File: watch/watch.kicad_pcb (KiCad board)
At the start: 2 copper layers, 92 parts, among them Q1 Q_NMOS_GSD, Q2 Q_NMOS_GSD, Q3 Q_NMOS_GSD, Q4 Q_NMOS_GSD, U1 STM32L071CBTx, Y1 Crystal

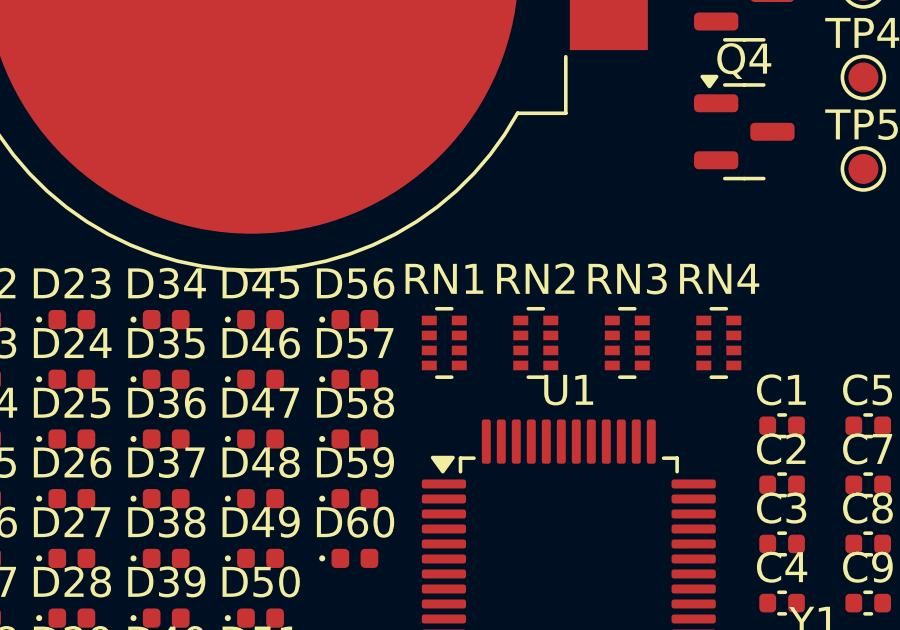
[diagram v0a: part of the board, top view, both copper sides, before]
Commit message: added unfinished footprint for DFN0606 FETs
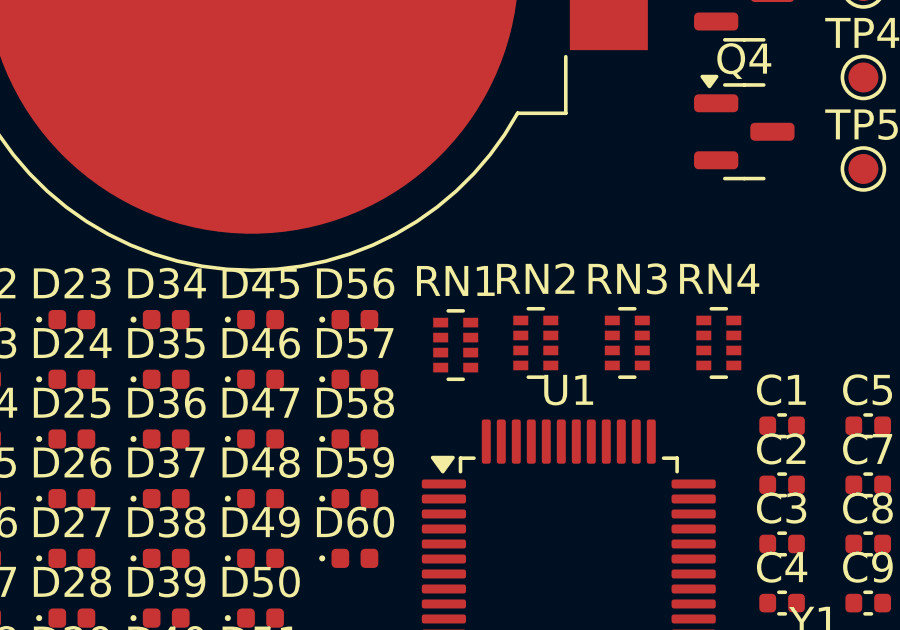
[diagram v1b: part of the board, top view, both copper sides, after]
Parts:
- moved RN1 0.39 mm to (159.8, 100.9)
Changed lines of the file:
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@@
 	(footprint "Resistor_SMD:R_Array_Concave_4x0402"
 		(layer "F.Cu")
-		(at 159.37 100.83)
+		(at 159.75 100.9)
 		(descr "Thick Film Chip Resistor Array, Wave soldering, Vishay CRA04P (see cra04p.pdf)")
 		(tags "resistor array")

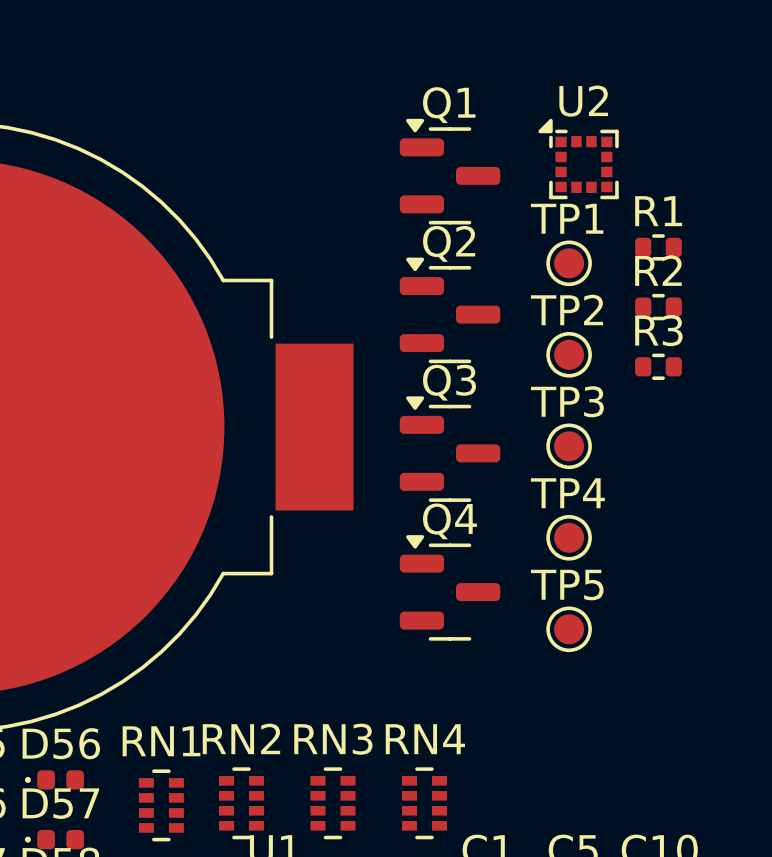
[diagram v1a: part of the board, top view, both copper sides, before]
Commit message: added DFN0606 footprint
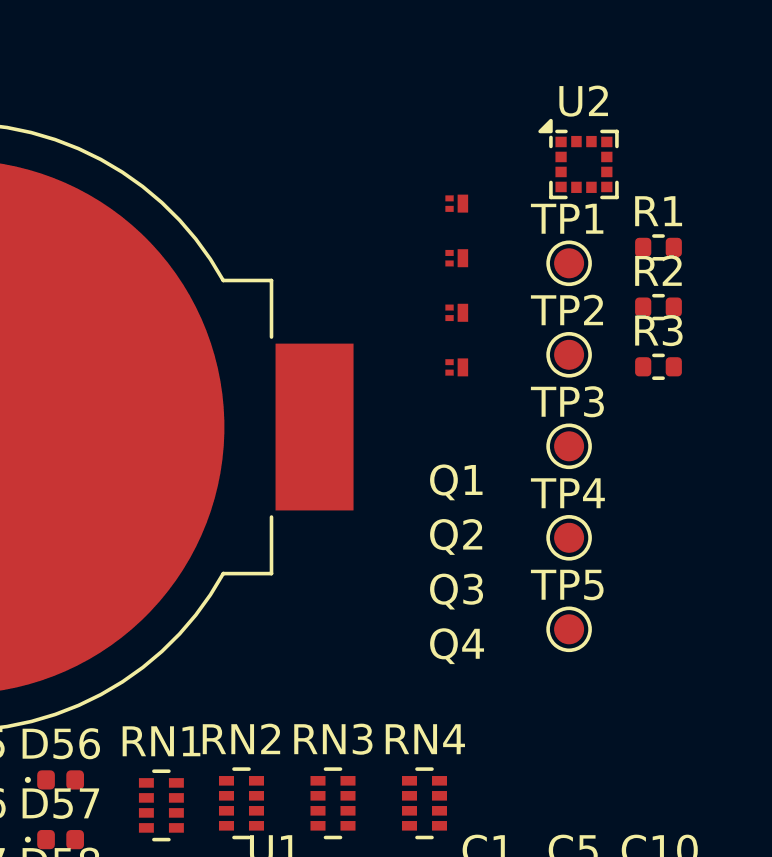
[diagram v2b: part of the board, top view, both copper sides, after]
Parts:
- Q1, Q2, Q3, Q4: value Q_NMOS_GSD -> DMN2991UFZ; footprint Package_TO_SOT_SMD:SOT-23 -> DFN0603:DFN0606
- moved Q4 7.49 mm to (169.6, 86.3)
- moved Q3 4.69 mm to (169.6, 84.5)
- moved Q2 1.89 mm to (169.6, 82.7)
- moved Q1 0.95 mm to (169.6, 80.8)

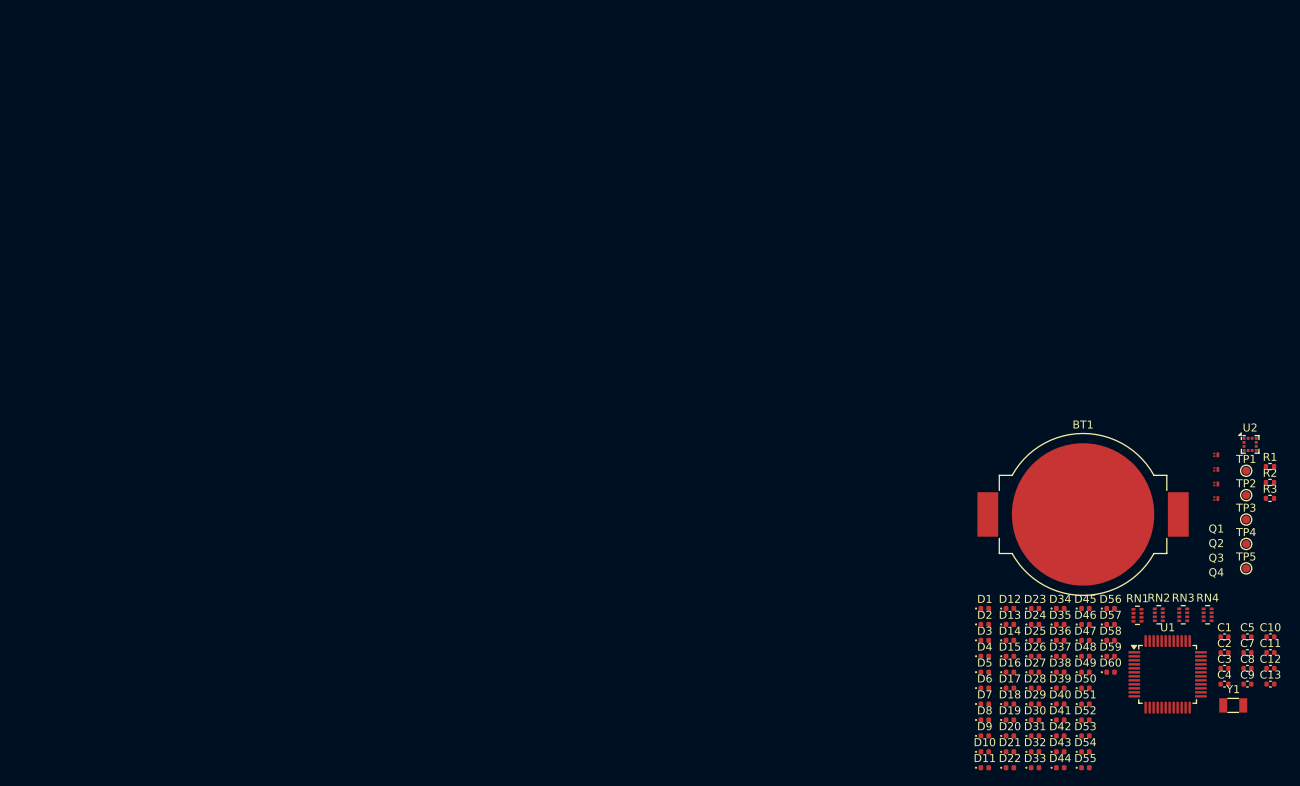
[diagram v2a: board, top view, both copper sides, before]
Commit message: removed low side FETs, started PCB
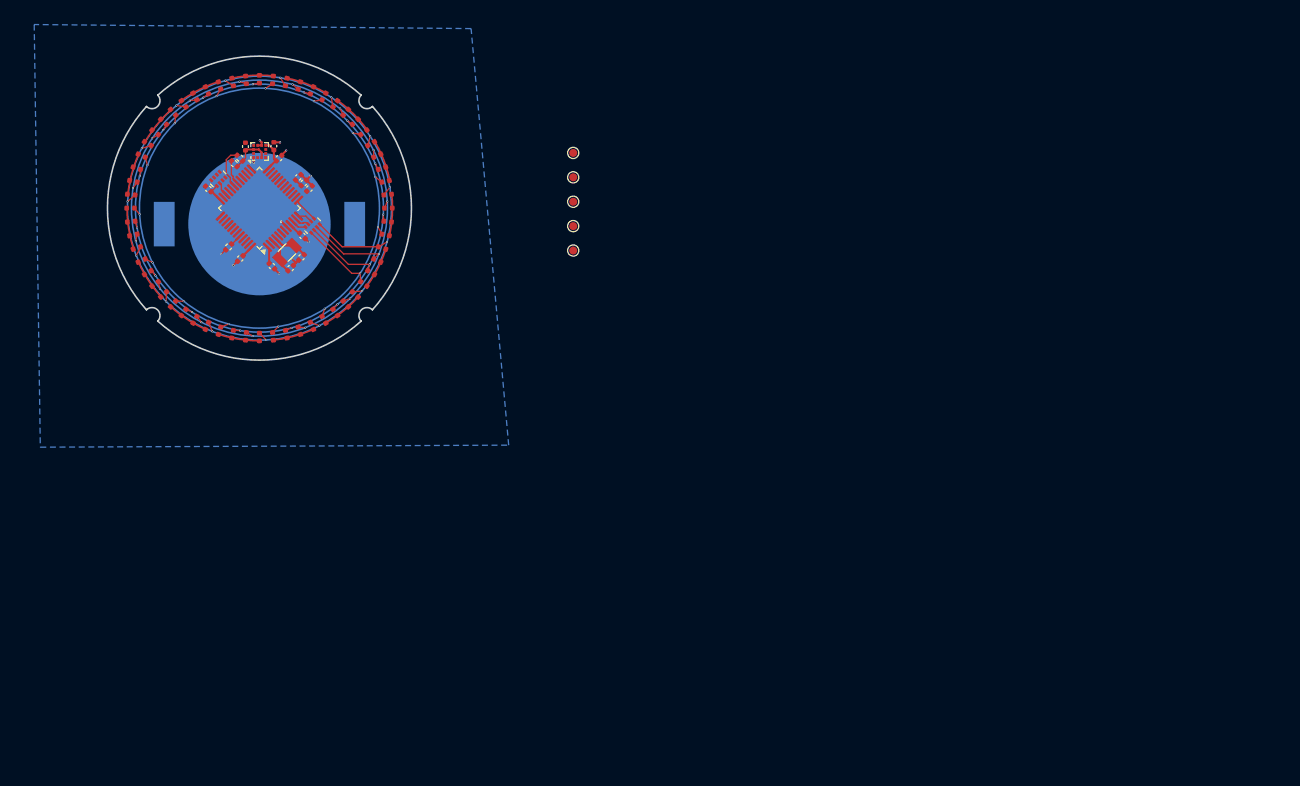
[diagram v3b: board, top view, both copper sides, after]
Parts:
- removed Q1, Q2, Q3, Q4: DMN2991UFZ, DFN0603:DFN0606
- removed RN2: 1M, Resistor_SMD:R_Array_Concave_4x0402
- removed RN3: 22, Resistor_SMD:R_Array_Concave_4x0402
- BT1: moved to B.Cu
- D1, D10, D11, D12, D13, D14, D15, D16, D17, D18, D19, D2, D20, D21, D22, D23, D24, D25, D26, D27, D28, D29, D3, D30, D31, D32, D33, D34, D35, D36, D37, D38, D39, D4, D40, D41, D42, D43, D44, D45, D46, D47, D48, D49, D5, D50, D51, D52, D53, D54, D55, D56, D57, D58, D59, D6, D60, D7, D8, D9: footprint LED_SMD:LED_0402_1005Metric -> LED_Without_Dot:LED402_without_dot
- RN1: value 1k -> 100
- Y1: value Crystal -> 3131M-32.768DTTLRRL
- moved C9 142.1 mm to (48.2, 42.3), turned to -90 degrees
- moved C4 141.3 mm to (43.6, 47.6), turned to -45 degrees
- moved C10 138.9 mm to (51.8, 42.2), turned to -90 degrees
- moved C12 136.1 mm to (54.9, 46.1), turned to -135 degrees
- moved C13 136.1 mm to (55.5, 46.9), turned to -135 degrees
- moved RN4 135.1 mm to (44.9, 46.4), turned to 135 degrees
- moved R2 135.0 mm to (47.5, 43.8), turned to 135 degrees
- moved R1 134.9 mm to (46.9, 44.5), turned to 135 degrees
- moved C5 134.5 mm to (47.6, 56.3), turned to 45 degrees
- moved C3 134.3 mm to (52.5, 43.8), turned to -135 degrees
- moved R3 133.9 mm to (46.1, 54.9), turned to -135 degrees
- moved C11 133.4 mm to (56.2, 47.5), turned to -135 degrees
- moved Y1 131.1 mm to (53.5, 55.5), turned to -135 degrees
- moved D11 130.6 mm to (37.0, 40.5), turned to 144 degrees
- moved D10 129.4 mm to (38.0, 39.2), turned to 138 degrees
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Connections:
- D10 pad 1: Net-(D1-K) -> Net-(D10-K)
- D10 pad 2: LED_SOURCE_COLUMN9 -> LED_SOURCE_COLUMN2
- D11 pad 1: Net-(D1-K) -> Net-(D11-K)
- D11 pad 2: LED_SOURCE_COLUMN10 -> LED_SOURCE_COLUMN2
- D12 pad 1: Net-(D1-K) -> Net-(D12-K)
- D12 pad 2: LED_SOURCE_COLUMN11 -> LED_SOURCE_COLUMN2
- D13 pad 2: LED_SOURCE_COLUMN12 -> LED_SOURCE_COLUMN3
- D14 pad 1: Net-(D1-K) -> Net-(D10-K)
- D14 pad 2: LED_SOURCE_COLUMN13 -> LED_SOURCE_COLUMN3
- D15 pad 1: Net-(D1-K) -> Net-(D11-K)
- D15 pad 2: LED_SOURCE_COLUMN14 -> LED_SOURCE_COLUMN3
- D16 pad 1: Net-(D16-K) -> Net-(D12-K)
- D16 pad 2: LED_SOURCE_COLUMN0 -> LED_SOURCE_COLUMN3
- D17 pad 1: Net-(D16-K) -> Net-(D1-K)
- D17 pad 2: LED_SOURCE_COLUMN1 -> LED_SOURCE_COLUMN4
- D18 pad 1: Net-(D16-K) -> Net-(D10-K)
- D18 pad 2: LED_SOURCE_COLUMN2 -> LED_SOURCE_COLUMN4
- D19 pad 1: Net-(D16-K) -> Net-(D11-K)
- D19 pad 2: LED_SOURCE_COLUMN3 -> LED_SOURCE_COLUMN4
- D2 pad 1: Net-(D1-K) -> Net-(D10-K)
- D2 pad 2: LED_SOURCE_COLUMN1 -> LED_SOURCE_COLUMN0
- D20 pad 1: Net-(D16-K) -> Net-(D12-K)
- D21 pad 1: Net-(D16-K) -> Net-(D1-K)
- D22 pad 1: Net-(D16-K) -> Net-(D10-K)
- D22 pad 2: LED_SOURCE_COLUMN6 -> LED_SOURCE_COLUMN5
- D23 pad 1: Net-(D16-K) -> Net-(D11-K)
- D23 pad 2: LED_SOURCE_COLUMN7 -> LED_SOURCE_COLUMN5
- D24 pad 1: Net-(D16-K) -> Net-(D12-K)
- D24 pad 2: LED_SOURCE_COLUMN8 -> LED_SOURCE_COLUMN5
- D25 pad 1: Net-(D16-K) -> Net-(D1-K)
- D25 pad 2: LED_SOURCE_COLUMN9 -> LED_SOURCE_COLUMN6
- D26 pad 1: Net-(D16-K) -> Net-(D10-K)
- D26 pad 2: LED_SOURCE_COLUMN10 -> LED_SOURCE_COLUMN6
- D27 pad 1: Net-(D16-K) -> Net-(D11-K)
- D27 pad 2: LED_SOURCE_COLUMN11 -> LED_SOURCE_COLUMN6
- D28 pad 1: Net-(D16-K) -> Net-(D12-K)
- D28 pad 2: LED_SOURCE_COLUMN12 -> LED_SOURCE_COLUMN6
- D29 pad 1: Net-(D16-K) -> Net-(D1-K)
- D29 pad 2: LED_SOURCE_COLUMN13 -> LED_SOURCE_COLUMN7
- D3 pad 1: Net-(D1-K) -> Net-(D11-K)
- D3 pad 2: LED_SOURCE_COLUMN2 -> LED_SOURCE_COLUMN0
- D30 pad 1: Net-(D16-K) -> Net-(D10-K)
- D30 pad 2: LED_SOURCE_COLUMN14 -> LED_SOURCE_COLUMN7
- D31 pad 1: Net-(D31-K) -> Net-(D11-K)
- D31 pad 2: LED_SOURCE_COLUMN0 -> LED_SOURCE_COLUMN7
- D32 pad 1: Net-(D31-K) -> Net-(D12-K)
- D32 pad 2: LED_SOURCE_COLUMN1 -> LED_SOURCE_COLUMN7
- D33 pad 1: Net-(D31-K) -> Net-(D1-K)
- D33 pad 2: LED_SOURCE_COLUMN2 -> LED_SOURCE_COLUMN8
- D34 pad 1: Net-(D31-K) -> Net-(D10-K)
- D34 pad 2: LED_SOURCE_COLUMN3 -> LED_SOURCE_COLUMN8
- D35 pad 1: Net-(D31-K) -> Net-(D11-K)
- D35 pad 2: LED_SOURCE_COLUMN4 -> LED_SOURCE_COLUMN8
- D36 pad 1: Net-(D31-K) -> Net-(D12-K)
- D36 pad 2: LED_SOURCE_COLUMN5 -> LED_SOURCE_COLUMN8
- D37 pad 1: Net-(D31-K) -> Net-(D1-K)
- D37 pad 2: LED_SOURCE_COLUMN6 -> LED_SOURCE_COLUMN9
- D38 pad 1: Net-(D31-K) -> Net-(D10-K)
- D38 pad 2: LED_SOURCE_COLUMN7 -> LED_SOURCE_COLUMN9
- D39 pad 1: Net-(D31-K) -> Net-(D11-K)
- D39 pad 2: LED_SOURCE_COLUMN8 -> LED_SOURCE_COLUMN9
- D4 pad 1: Net-(D1-K) -> Net-(D12-K)
- D4 pad 2: LED_SOURCE_COLUMN3 -> LED_SOURCE_COLUMN0
- D40 pad 1: Net-(D31-K) -> Net-(D12-K)
- D41 pad 1: Net-(D31-K) -> Net-(D1-K)
- D42 pad 1: Net-(D31-K) -> Net-(D10-K)
- D42 pad 2: LED_SOURCE_COLUMN11 -> LED_SOURCE_COLUMN10
- D43 pad 1: Net-(D31-K) -> Net-(D11-K)
- D43 pad 2: LED_SOURCE_COLUMN12 -> LED_SOURCE_COLUMN10
- D44 pad 1: Net-(D31-K) -> Net-(D12-K)
- D44 pad 2: LED_SOURCE_COLUMN13 -> LED_SOURCE_COLUMN10
- D45 pad 1: Net-(D31-K) -> Net-(D1-K)
- D45 pad 2: LED_SOURCE_COLUMN14 -> LED_SOURCE_COLUMN11
- D46 pad 1: Net-(D46-K) -> Net-(D10-K)
- D46 pad 2: LED_SOURCE_COLUMN0 -> LED_SOURCE_COLUMN11
- D47 pad 1: Net-(D46-K) -> Net-(D11-K)
- D47 pad 2: LED_SOURCE_COLUMN1 -> LED_SOURCE_COLUMN11
- D48 pad 1: Net-(D46-K) -> Net-(D12-K)
- D48 pad 2: LED_SOURCE_COLUMN2 -> LED_SOURCE_COLUMN11
- D49 pad 1: Net-(D46-K) -> Net-(D1-K)
- D49 pad 2: LED_SOURCE_COLUMN3 -> LED_SOURCE_COLUMN12
- D5 pad 2: LED_SOURCE_COLUMN4 -> LED_SOURCE_COLUMN1
- D50 pad 1: Net-(D46-K) -> Net-(D10-K)
- D50 pad 2: LED_SOURCE_COLUMN4 -> LED_SOURCE_COLUMN12
- D51 pad 1: Net-(D46-K) -> Net-(D11-K)
- D51 pad 2: LED_SOURCE_COLUMN5 -> LED_SOURCE_COLUMN12
- D52 pad 1: Net-(D46-K) -> Net-(D12-K)
- D52 pad 2: LED_SOURCE_COLUMN6 -> LED_SOURCE_COLUMN12
- D53 pad 1: Net-(D46-K) -> Net-(D1-K)
- D53 pad 2: LED_SOURCE_COLUMN7 -> LED_SOURCE_COLUMN13
- D54 pad 1: Net-(D46-K) -> Net-(D10-K)
- D54 pad 2: LED_SOURCE_COLUMN8 -> LED_SOURCE_COLUMN13
- D55 pad 1: Net-(D46-K) -> Net-(D11-K)
- D55 pad 2: LED_SOURCE_COLUMN9 -> LED_SOURCE_COLUMN13
- D56 pad 1: Net-(D46-K) -> Net-(D12-K)
- D56 pad 2: LED_SOURCE_COLUMN10 -> LED_SOURCE_COLUMN13
- D57 pad 1: Net-(D46-K) -> Net-(D1-K)
- D57 pad 2: LED_SOURCE_COLUMN11 -> LED_SOURCE_COLUMN14
- D58 pad 1: Net-(D46-K) -> Net-(D10-K)
- D58 pad 2: LED_SOURCE_COLUMN12 -> LED_SOURCE_COLUMN14
- D59 pad 1: Net-(D46-K) -> Net-(D11-K)
- D59 pad 2: LED_SOURCE_COLUMN13 -> LED_SOURCE_COLUMN14
- D6 pad 1: Net-(D1-K) -> Net-(D10-K)
- D6 pad 2: LED_SOURCE_COLUMN5 -> LED_SOURCE_COLUMN1
- D60 pad 1: Net-(D46-K) -> Net-(D12-K)
- D7 pad 1: Net-(D1-K) -> Net-(D11-K)
- D7 pad 2: LED_SOURCE_COLUMN6 -> LED_SOURCE_COLUMN1
- D8 pad 1: Net-(D1-K) -> Net-(D12-K)
- D8 pad 2: LED_SOURCE_COLUMN7 -> LED_SOURCE_COLUMN1
- D9 pad 2: LED_SOURCE_COLUMN8 -> LED_SOURCE_COLUMN2
- RN1 pad 1: Net-(Q1-D) -> LED_SINK_ROW3_GPIO
- RN1 pad 2: Net-(Q2-D) -> LED_SINK_ROW2_GPIO
- RN1 pad 3: Net-(Q3-D) -> LED_SINK_ROW1_GPIO
- RN1 pad 4: Net-(Q4-D) -> LED_SINK_ROW0_GPIO
- RN1 pad 5: Net-(D46-K) -> Net-(D1-K)
- RN1 pad 6: Net-(D31-K) -> Net-(D10-K)
- RN1 pad 7: Net-(D16-K) -> Net-(D11-K)
- RN1 pad 8: Net-(D1-K) -> Net-(D12-K)
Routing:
- net Net-(D12-K): track 0.00 -> 26.7 mm, vias 0 -> 15
- net Net-(D1-K): track 0.00 -> 23.5 mm, vias 0 -> 15
- net Net-(D11-K): track 0.00 -> 22.8 mm, vias 0 -> 15
- net Net-(D10-K): track 0.00 -> 21.1 mm, vias 0 -> 15
- net VDD: track 0.00 -> 18.5 mm
- net GND: track 0.00 -> 11.8 mm, vias 0 -> 11
- net IMU_SDA: track 0.00 -> 5.29 mm
- net Net-(U1-PC14): track 0.00 -> 4.43 mm
- net Net-(U1-PC15): track 0.00 -> 4.35 mm
- net LED_SINK_ROW3_GPIO: track 0.00 -> 3.11 mm
- net IMU_SCL: track 0.00 -> 3.10 mm
- net LED_SINK_ROW1_GPIO: track 0.00 -> 1.91 mm
- net LED_SINK_ROW0_GPIO: track 0.00 -> 1.85 mm
- net LED_SINK_ROW2_GPIO: track 0.00 -> 1.85 mm
- net SWDIO: track 0.00 -> 1.74 mm
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- added copper zone on B.Cu, net GND
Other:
- board outline added: 38 x 38 mm
- copper layers 2 -> 4

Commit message: V1.6 basic layout done
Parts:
- removed RN1: 100, Resistor_SMD:R_Array_Concave_4x0402
- removed RN4: 22, Resistor_SMD:R_Array_Concave_4x0402
- added R10: 22, Resistor_SMD:R_0603_1608Metric, F.Cu at (50.2, 59.6)
- added R4: 100, Resistor_SMD:R_0603_1608Metric, F.Cu at (56.9, 40.9)
- added R5: 100, Resistor_SMD:R_0603_1608Metric, F.Cu at (58.0, 42.0)
- added R6: 100, Resistor_SMD:R_0603_1608Metric, F.Cu at (59.1, 43.1)
- added R7: 100, Resistor_SMD:R_0603_1608Metric, F.Cu at (60.2, 44.2)
- added R8: 22, Resistor_SMD:R_0603_1608Metric, F.Cu at (42.6, 52.1)
- added R9: 22, Resistor_SMD:R_0603_1608Metric, F.Cu at (43.7, 53.2)
- C1, C10, C11, C12, C13, C2, C3, C4, C5, C7, C8, C9: footprint Capacitor_SMD:C_0402_1005Metric -> Capacitor_SMD:C_0603_1608Metric
- D1, D10, D11, D12, D13, D14, D15, D16, D17, D18, D19, D2, D20, D21, D22, D23, D24, D25, D26, D27, D28, D29, D3, D30, D31, D32, D33, D34, D35, D36, D37, D38, D39, D4, D40, D41, D42, D43, D44, D45, D46, D47, D48, D49, D5, D50, D51, D52, D53, D54, D55, D56, D57, D58, D59, D6, D60, D7, D8, D9: footprint LED_Without_Dot:LED402_without_dot -> LED_SMD:LED_0603_1608Metric
- R1, R2, R3: footprint Resistor_SMD:R_0402_1005Metric -> Resistor_SMD:R_0603_1608Metric
- TP1, TP2, TP3, TP4, TP5: footprint TestPoint:TestPoint_Pad_D1.0mm -> TestPoint:TestPoint_Pad_D2.0mm; moved to B.Cu
- moved TP5 52.0 mm to (38.3, 45.1)
- moved TP4 50.2 mm to (40.1, 42.0)
- moved TP3 47.3 mm to (42.9, 39.8)
- moved TP2 44.0 mm to (45.9, 38.2)
- moved TP1 40.1 mm to (49.5, 37.6)
- moved C12 14.9 mm to (40.4, 50.0), turned to 45 degrees
- moved C13 14.6 mm to (41.5, 51.0), turned to 45 degrees
- moved C4 13.0 mm to (51.7, 57.8), turned to 135 degrees
- moved C11 12.9 mm to (48.0, 57.4), turned to 45 degrees
- moved C5 10.1 mm to (43.3, 47.2), turned to -45 degrees
- moved C1 4.72 mm to (46.9, 56.4), turned to 45 degrees
- moved R3 4.67 mm to (49.1, 58.5), turned to 45 degrees
- moved R2 3.95 mm to (44.4, 46.1), turned to -45 degrees
- moved C10 3.80 mm to (48.0, 42.5), turned to 90 degrees
- moved C9 2.69 mm to (50.0, 40.3), turned to 0 degrees
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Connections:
- TP1 pad 1: Net-(RN4-R1.2) -> VDD
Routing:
- net VDD: track 18.5 -> 123.9 mm, vias 0 -> 11
- net GND: track 11.8 -> 76.6 mm, vias 11 -> 13
- net Net-(R10-Pad2): track 0.00 -> 32.7 mm, vias 0 -> 1
- net IMU_WAKEUP_INTERRUPT: track 0.00 -> 30.6 mm, vias 0 -> 2
- net LED_SOURCE_COLUMN2: track 0.00 -> 25.2 mm
- net LED_SOURCE_COLUMN12: track 0.00 -> 24.5 mm, vias 0 -> 2
- net Net-(R8-Pad2): track 0.00 -> 22.1 mm, vias 0 -> 1
- net LED_SOURCE_COLUMN9: track 0.00 -> 21.2 mm
- net Net-(R9-Pad2): track 0.00 -> 21.0 mm, vias 0 -> 1
- net LED_SOURCE_COLUMN11: track 0.00 -> 20.2 mm, vias 0 -> 2
- net LED_SOURCE_COLUMN14: track 0.00 -> 20.2 mm, vias 0 -> 2
- net LED_SOURCE_COLUMN13: track 0.00 -> 19.9 mm, vias 0 -> 2
- net LED_SOURCE_COLUMN10: track 0.00 -> 19.8 mm, vias 0 -> 2
- net LED_SOURCE_COLUMN1: track 0.00 -> 19.7 mm
- net LED_SOURCE_COLUMN8: track 0.00 -> 17.6 mm
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- added copper zone on F.Cu, net VDD

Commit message: V1.6 done?
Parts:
- D1, D10, D11, D12, D13, D14, D15, D16, D17, D18, D19, D2, D20, D21, D22, D23, D24, D25, D26, D27, D28, D29, D3, D30, D31, D32, D33, D34, D35, D36, D37, D38, D39, D4, D40, D41, D42, D43, D44, D45, D46, D47, D48, D49, D5, D50, D51, D52, D53, D54, D55, D56, D57, D58, D59, D6, D60, D7, D8, D9: footprint LED_SMD:LED_0603_1608Metric -> LED_Without_Dot:0603
- R4, R5, R6, R7: value 100 -> 160
- U2: value ~ -> BOSCH BMA400
- moved D3 39.4 mm to (52.4, 73.2), turned to 96 degrees
- moved D2 39.4 mm to (50.7, 73.3), turned to 90 degrees
- moved D4 39.4 mm to (54.1, 72.9), turned to 102 degrees
- moved D1 39.3 mm to (49.0, 73.2), turned to 84 degrees
- moved D5 39.3 mm to (55.7, 72.5), turned to 108 degrees
- moved D60 39.1 mm to (47.4, 72.9), turned to 78 degrees
- moved D6 39.1 mm to (57.3, 71.9), turned to 114 degrees
- moved D59 38.9 mm to (45.7, 72.5), turned to 72 degrees
- moved D7 38.9 mm to (58.8, 71.1), turned to 120 degrees
- moved D58 38.6 mm to (44.2, 71.9), turned to 66 degrees
- moved D8 38.6 mm to (60.2, 70.2), turned to 126 degrees
- moved D57 38.3 mm to (42.7, 71.1), turned to 60 degrees
- moved D9 38.3 mm to (61.5, 69.1), turned to 132 degrees
- moved D56 37.9 mm to (41.2, 70.2), turned to 54 degrees
- moved D10 37.9 mm to (62.7, 67.9), turned to 138 degrees
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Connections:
- U1 pad 17: unconnected-(U1-PA7-Pad17) -> VDD
- U2 pad 10: unconnected-(U2-NC-Pad10) -> VDD
- U2 pad 11: VDD -> unconnected-(U2-PS-Pad11)
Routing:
- net IMU_WAKEUP_INTERRUPT: track 30.6 -> 40.8 mm, vias 2 -> 6
- net VDD: track 123.9 -> 133.7 mm, vias 11 -> 13
- net Net-(D12-K): track 18.3 -> 25.3 mm, vias 16 -> 15
- net LED_SINK_ROW3_GPIO: track 9.00 -> 2.11 mm
- net Net-(D1-K): track 30.1 -> 36.9 mm
- net LED_SINK_ROW2_GPIO: track 11.1 -> 4.75 mm
- net LED_SINK_ROW1_GPIO: track 10.9 -> 4.86 mm
- net Net-(D11-K): track 18.9 -> 24.9 mm, vias 16 -> 15
- net Net-(D10-K): track 22.6 -> 28.5 mm, vias 16 -> 15
- net LED_SINK_ROW0_GPIO: track 11.4 -> 5.58 mm
- net GND: track 76.6 -> 82.1 mm, vias 13 -> 17
- net LED_SOURCE_COLUMN11: track 20.2 -> 16.7 mm
- net LED_SOURCE_COLUMN13: track 19.9 -> 23.4 mm, vias 2 -> 5
- net LED_SOURCE_COLUMN14: track 20.2 -> 22.7 mm
- net LED_SOURCE_COLUMN4: track 12.3 -> 14.3 mm
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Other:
- copper layers 4 -> 2
- board text added: "GND"
- board text added: "JLCJLCJLCJLC"
- board text added: "NRST"
- board text added: "Rev 1.6 mrab"
- board text added: "SWCLK"
- board text added: "SWDIO"
- board text added: "VDD"
